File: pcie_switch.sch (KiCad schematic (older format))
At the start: 42 parts

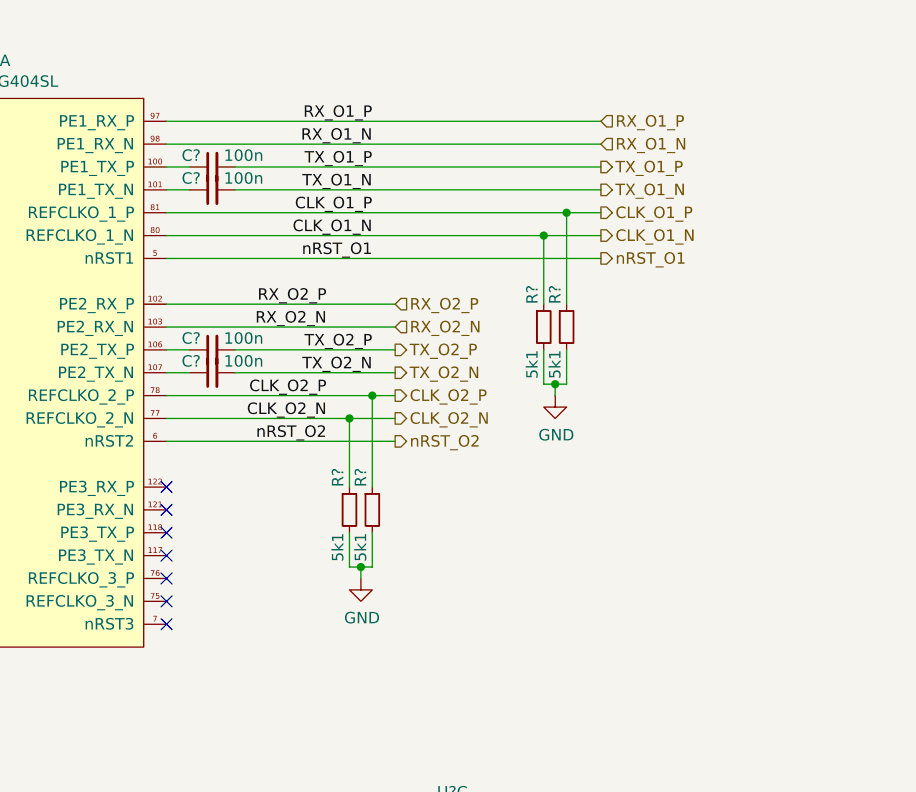
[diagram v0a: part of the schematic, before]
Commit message: sch: Add some PCIe doc and termination resistors
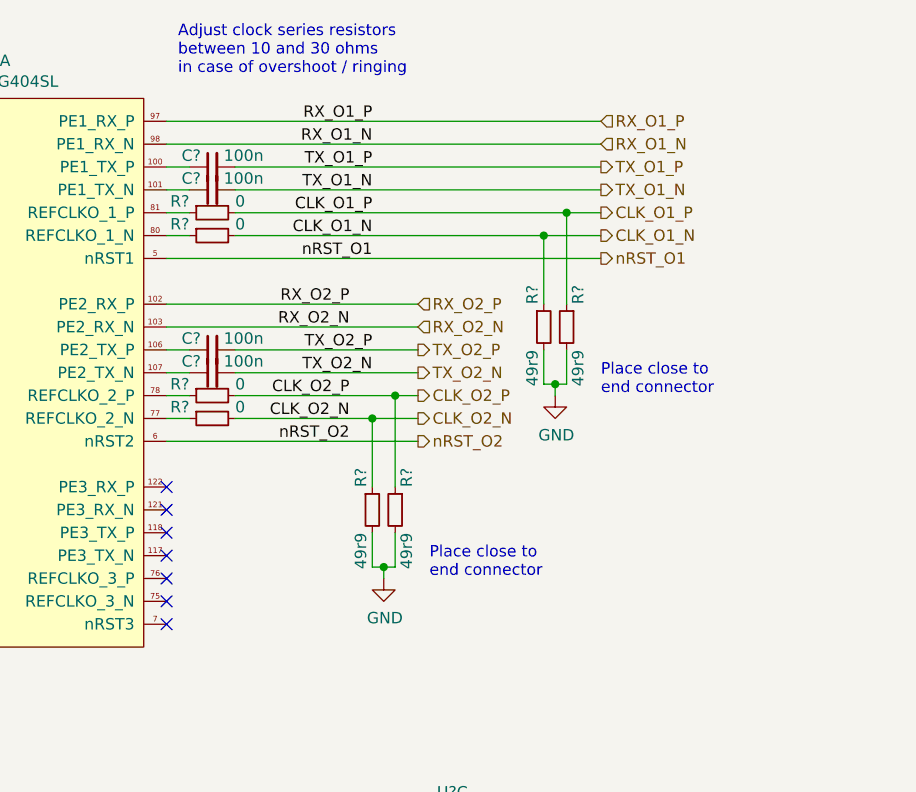
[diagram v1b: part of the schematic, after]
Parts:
- added R? (x4): 0, symbol Device:R_Small
- R? (x4): value 5k1 -> 49r9
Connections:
- net CLK_O1_N: now also R?.2; no longer U?.80 (REFCLKO_1_N)
- net CLK_O1_P: now also R?.2; no longer U?.81 (REFCLKO_1_P)
- net CLK_O2_N: now also R?.2; no longer U?.77 (REFCLKO_2_N)
- net CLK_O2_P: now also R?.2; no longer U?.78 (REFCLKO_2_P)
- new net: R?.1, U?.77 (REFCLKO_2_N)
- new net: R?.1, U?.78 (REFCLKO_2_P)
- new net: R?.1, U?.80 (REFCLKO_1_N)
- new net: R?.1, U?.81 (REFCLKO_1_P)
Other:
- note added: "Adjust clock series resistors\nbetween 10 and 30 ohms\nin case of overshoot / ringing"
- note added: "Place close to\nend connector"
- moved on the sheet: R?
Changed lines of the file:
@@
 Text HLabel 5700 1800 2    50   Output ~ 0
 TX_O1_N
-Wire Wire Line
-	5700 2000 5450 2000
 Text HLabel 5700 1900 2    50   Output ~ 0
 CLK_O1_P
@@
 CLK_O1_N
 Wire Wire Line
-	5700 1900 5550 1900
-Wire Wire Line
 	5700 2100 3800 2100
 Text HLabel 5700 2100 2    50   Output ~ 0
@@
 nRST_O1
 Wire Wire Line
-	3800 2300 4800 2300
-Text Label 4500 2300 2    50   ~ 0
+	3800 2300 4900 2300
+Text Label 4600 2300 2    50   ~ 0
 RX_O2_P
 Wire Wire Line
-	3800 2400 4800 2400
-Text Label 4500 2400 2    50   ~ 0
+	3800 2400 4900 2400
+Text Label 4600 2400 2    50   ~ 0
 RX_O2_N
 Wire Wire Line
-	4100 2500 4800 2500
+	4100 2500 4900 2500
 Text Label 4700 2500 2    50   ~ 0
 TX_O2_P
 Wire Wire Line
-	4100 2600 4800 2600
+	4100 2600 4900 2600
 Text Label 4700 2600 2    50   ~ 0
 TX_O2_N
-Text HLabel 4800 2300 2    50   Input ~ 0
+Text HLabel 4900 2300 2    50   Input ~ 0
 RX_O2_P
-Text HLabel 4800 2400 2    50   Input ~ 0
+Text HLabel 4900 2400 2    50   Input ~ 0
 RX_O2_N
-Text HLabel 4800 2500 2    50   Output ~ 0
+Text HLabel 4900 2500 2    50   Output ~ 0
 TX_O2_P
-Text HLabel 4800 2600 2    50   Output ~ 0
+Text HLabel 4900 2600 2    50   Output ~ 0
 TX_O2_N
-Wire Wire Line
-	4800 2800 4600 2800
-Text HLabel 4800 2700 2    50   Output ~ 0
+Text HLabel 4900 2700 2    50   Output ~ 0
 CLK_O2_P
-Text HLabel 4800 2800 2    50   Output ~ 0
+Text HLabel 4900 2800 2    50   Output ~ 0
 CLK_O2_N
-Text Label 4500 2700 2    50   ~ 0
+Text Label 4600 2700 2    50   ~ 0
 CLK_O2_P
-Text Label 4500 2800 2    50   ~ 0
+Text Label 4600 2800 2    50   ~ 0
 CLK_O2_N
 Wire Wire Line
-	4800 2700 4700 2700
-Wire Wire Line
-	4800 2900 3800 2900
-Text HLabel 4800 2900 2    50   Output ~ 0
+	4900 2900 3800 2900
+Text HLabel 4900 2900 2    50   Output ~ 0
 nRST_O2
-Text Label 4500 2900 2    50   ~ 0
+Text Label 4600 2900 2    50   ~ 0
 nRST_O2
 NoConn ~ 3800 3100
@@
 L Device:R_Small R?
 U 1 1 5D930A7A
-P 4600 3200
-F 0 "R?" V 4550 3300 50  0000 L CNN
-F 1 "5k1" V 4550 3100 50  0000 R CNN
-F 2 "" H 4600 3200 50  0001 C CNN
-F 3 "~" H 4600 3200 50  0001 C CNN
-	1    4600 3200
-	1    0    0    -1
-$EndComp
-$Comp
-L Device:R_Small R?
-U 1 1 5D9310A8
 P 4700 3200
 F 0 "R?" V 4650 3300 50  0000 L CNN
-F 1 "5k1" V 4650 3100 50  0000 R CNN
+F 1 "49r9" V 4650 3100 50  0000 R CNN
 F 2 "" H 4700 3200 50  0001 C CNN
 F 3 "~" H 4700 3200 50  0001 C CNN
@@
 	1    0    0    -1
 $EndComp
-Wire Wire Line
-	4600 3100 4600 2800
-Connection ~ 4600 2800
-Wire Wire Line
-	4600 2800 3800 2800
-Wire Wire Line
-	4700 3100 4700 2700
-Connection ~ 4700 2700
-Wire Wire Line
-	4700 2700 3800 2700
-Wire Wire Line
-	4600 3300 4600 3450
-Wire Wire Line
-	4600 3450 4650 3450
-Wire Wire Line
-	4700 3450 4700 3300
-Wire Wire Line
-	4650 3450 4650 3500
-Connection ~ 4650 3450
-Wire Wire Line
-	4650 3450 4700 3450
+$Comp
+L Device:R_Small R?
+U 1 1 5D9310A8
+P 4800 3200
+F 0 "R?" V 4750 3300 50  0000 L CNN
+F 1 "49r9" V 4750 3100 50  0000 R CNN
+F 2 "" H 4800 3200 50  0001 C CNN
+F 3 "~" H 4800 3200 50  0001 C CNN
+	1    4800 3200
+	-1   0    0    -1
+$EndComp
+Wire Wire Line
+	4700 3100 4700 2800
+Wire Wire Line
+	4800 3100 4800 2700
+Wire Wire Line
+	4700 3300 4700 3450
+Wire Wire Line
+	4700 3450 4750 3450
+Wire Wire Line
+	4800 3450 4800 3300
+Wire Wire Line
+	4750 3450 4750 3500
+Connection ~ 4750 3450
+Wire Wire Line
+	4750 3450 4800 3450
 $Comp
 L power:GND #PWR?
 U 1 1 5D97FC67
-P 4650 3500
-F 0 "#PWR?" H 4650 3250 50  0001 C CNN
-F 1 "GND" H 4655 3327 50  0000 C CNN
-F 2 "" H 4650 3500 50  0001 C CNN
-F 3 "" H 4650 3500 50  0001 C CNN
-	1    4650 3500
+P 4750 3500
+F 0 "#PWR?" H 4750 3250 50  0001 C CNN
+F 1 "GND" H 4755 3327 50  0000 C CNN
+F 2 "" H 4750 3500 50  0001 C CNN
+F 3 "" H 4750 3500 50  0001 C CNN
+	1    4750 3500
 	1    0    0    -1
 $EndComp
@@
 P 5450 2400
 F 0 "R?" V 5400 2500 50  0000 L CNN
-F 1 "5k1" V 5400 2300 50  0000 R CNN
+F 1 "49r9" V 5400 2300 50  0000 R CNN
 F 2 "" H 5450 2400 50  0001 C CNN
 F 3 "~" H 5450 2400 50  0001 C CNN
@@
 P 5550 2400
 F 0 "R?" V 5500 2500 50  0000 L CNN
-F 1 "5k1" V 5500 2300 50  0000 R CNN
+F 1 "49r9" V 5500 2300 50  0000 R CNN
 F 2 "" H 5550 2400 50  0001 C CNN
 F 3 "~" H 5550 2400 50  0001 C CNN
 	1    5550 2400
-	1    0    0    -1
+	-1   0    0    -1
 $EndComp
 Wire Wire Line
@@
 	1    0    0    -1
 $EndComp
+Text Notes 5700 2700 0    50   ~ 0
+Place close to\nend connector
+Text Notes 4950 3500 0    50   ~ 0
+Place close to\nend connector
+Wire Wire Line
+	5450 2000 4100 2000
+Wire Wire Line
+	5550 1900 4100 1900
+Wire Wire Line
+	5450 2000 5700 2000
+Wire Wire Line
+	5550 1900 5700 1900
 Connection ~ 5450 2000
-Wire Wire Line
-	5450 2000 3800 2000
 Connection ~ 5550 1900
-Wire Wire Line
-	5550 1900 3800 1900
+$Comp
+L Device:R_Small R?
+U 1 1 5DBCB726
+P 4000 2000
+F 0 "R?" V 3950 2100 50  0000 L CNN
+F 1 "0" V 3950 1900 50  0000 R CNN
+F 2 "" H 4000 2000 50  0001 C CNN
+F 3 "~" H 4000 2000 50  0001 C CNN
+	1    4000 2000
+	0    -1   1    0
+$EndComp
+$Comp
+L Device:R_Small R?
+U 1 1 5DBDCE29
+P 4000 1900
+F 0 "R?" V 3950 2000 50  0000 L CNN
+F 1 "0" V 3950 1800 50  0000 R CNN
+F 2 "" H 4000 1900 50  0001 C CNN
+F 3 "~" H 4000 1900 50  0001 C CNN
+	1    4000 1900
+	0    -1   1    0
+$EndComp
+Wire Wire Line
+	3800 1900 3900 1900
+Wire Wire Line
+	3800 2000 3900 2000
+$Comp
+L Device:R_Small R?
+U 1 1 5DC36BA7
+P 4000 2700
+F 0 "R?" V 3950 2800 50  0000 L CNN
+F 1 "0" V 3950 2600 50  0000 R CNN
+F 2 "" H 4000 2700 50  0001 C CNN
+F 3 "~" H 4000 2700 50  0001 C CNN
+	1    4000 2700
+	0    -1   1    0
+$EndComp
+$Comp
+L Device:R_Small R?
+U 1 1 5DC36C3F
+P 4000 2800
+F 0 "R?" V 3950 2900 50  0000 L CNN
+F 1 "0" V 3950 2700 50  0000 R CNN
+F 2 "" H 4000 2800 50  0001 C CNN
+F 3 "~" H 4000 2800 50  0001 C CNN
+	1    4000 2800
+	0    -1   1    0
+$EndComp
+Wire Wire Line
+	3800 2800 3900 2800
+Wire Wire Line
+	3900 2700 3800 2700
+Connection ~ 4700 2800
+Wire Wire Line
+	4700 2800 4900 2800
+Connection ~ 4800 2700
+Wire Wire Line
+	4800 2700 4900 2700
+Wire Wire Line
+	4100 2800 4700 2800
+Wire Wire Line
+	4100 2700 4800 2700
+Text Notes 3850 1300 0    50   ~ 0
+Adjust clock series resistors\nbetween 10 and 30 ohms\nin case of overshoot / ringing
 $EndSCHEMATC
